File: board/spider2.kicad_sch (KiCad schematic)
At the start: 101 parts, among them J1 NRJ6HH, J10 PJ-320A, J11 PJ359, J12 PJ359, J13 PJ359, J14 PJ359, J15 PJ359, J16 PJ359, J19 PJ359, J2 NRJ6HH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

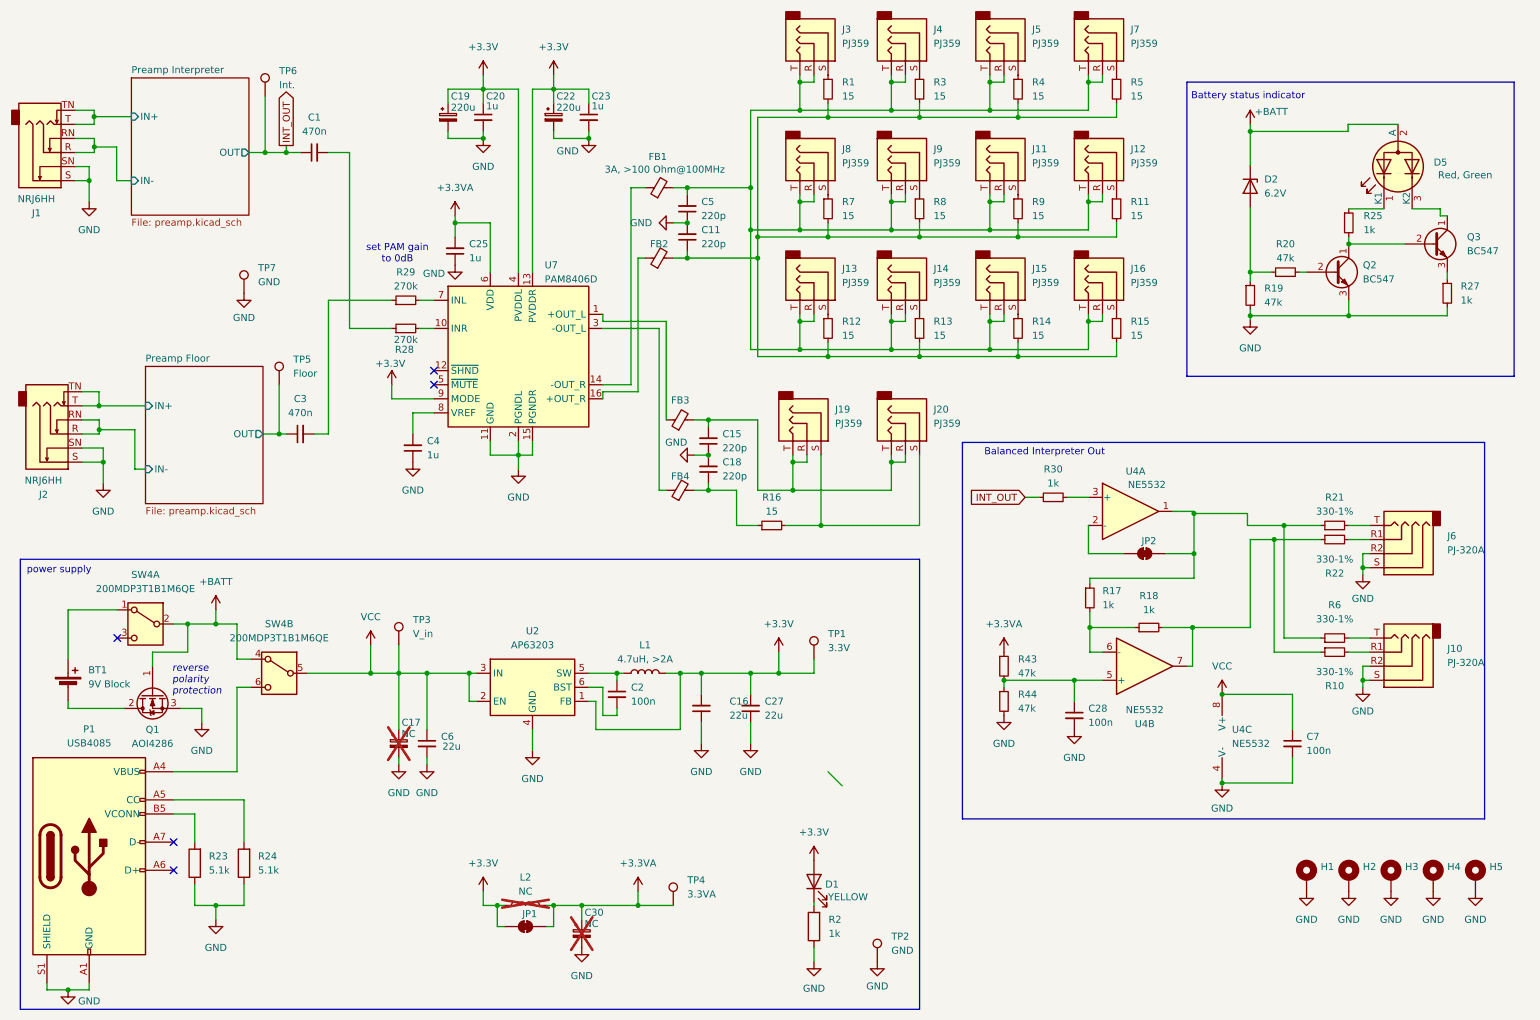
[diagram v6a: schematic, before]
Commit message: reduce balanced out volume, 3.3V supply on SMD for lower emissions
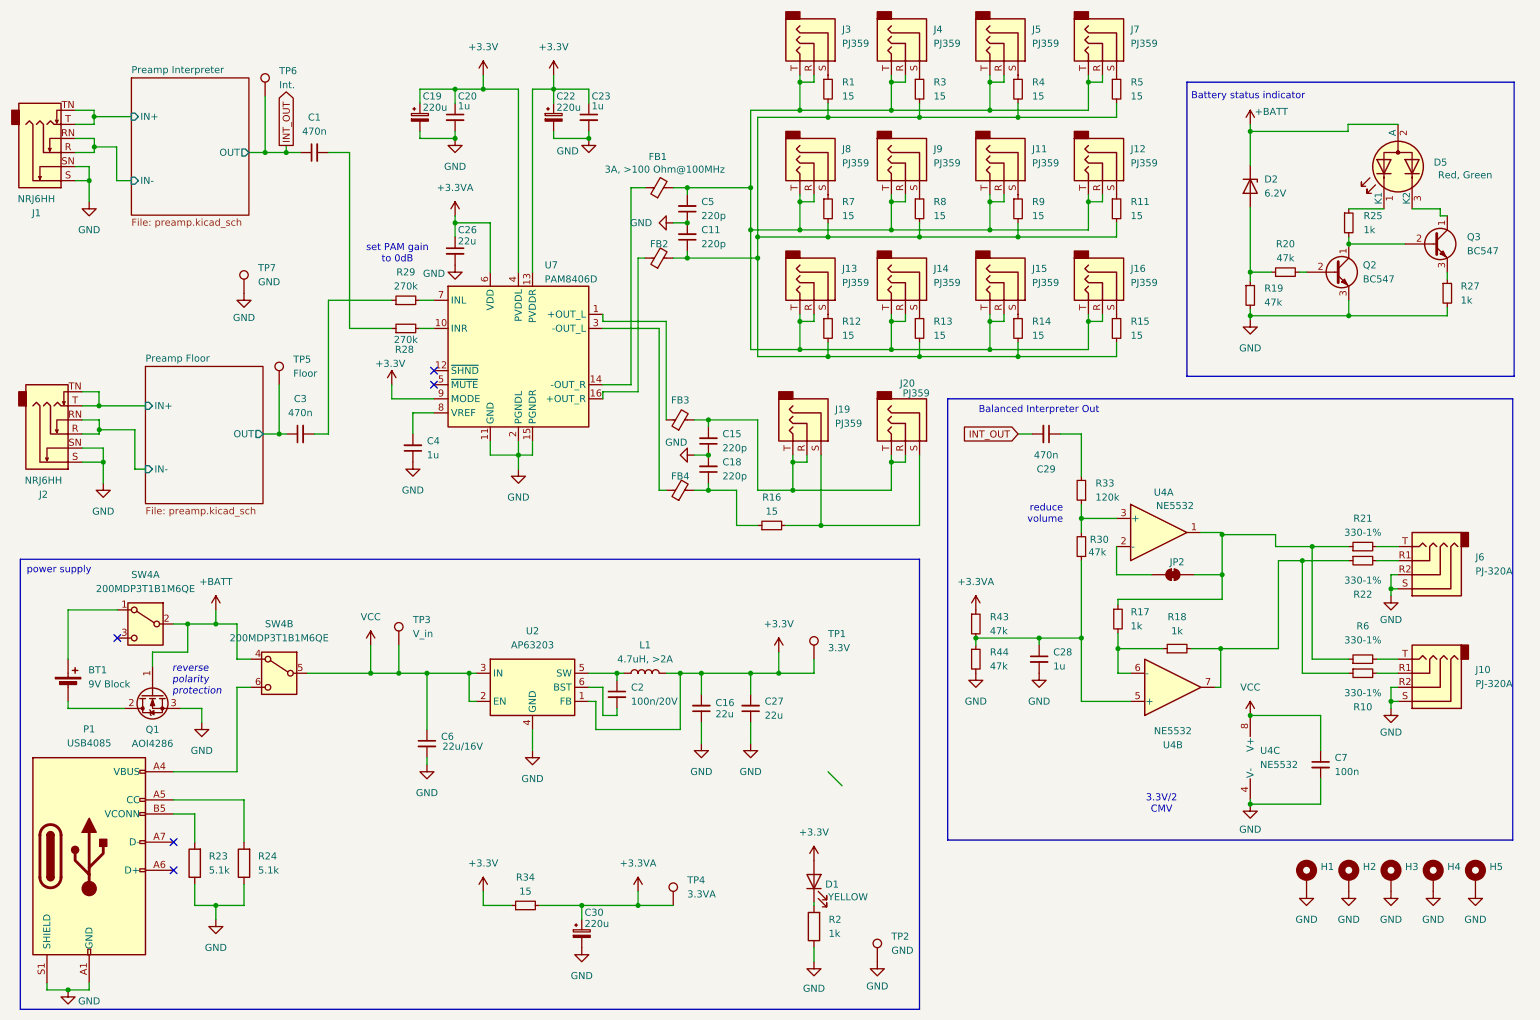
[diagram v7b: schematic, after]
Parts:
- removed C17: NC, Capacitor_THT:CP_Radial_D6.3mm_P2.50mm, symbol Device:C_Polarized_Small
- removed C25: 1u, Capacitor_THT:C_Disc_D4.3mm_W1.9mm_P5.00mm, symbol Device:C_Small
- removed JP1: SolderJumper_2_Bridged, Jumper:SolderJumper-2_P1.3mm_Bridged_RoundedPad1.0x1.5mm, symbol Jumper:SolderJumper_2_Bridged
- removed L2: NC, Inductor_THT:L_Axial_L5.3mm_D2.2mm_P10.16mm_Horizontal_Vishay_IM-1, symbol Device:L
- added C26: 22u, Capacitor_SMD:C_1206_3216Metric_Pad1.33x1.80mm_HandSolder, symbol Device:C_Small
- added C29: 470n, Capacitor_THT:C_Disc_D5.1mm_W3.2mm_P5.00mm, symbol Device:C_Small
- added R33: 120k, Resistor_THT:R_Axial_DIN0207_L6.3mm_D2.5mm_P10.16mm_Horizontal, symbol Device:R_Small
- added R34: 15, Resistor_THT:R_Axial_DIN0207_L6.3mm_D2.5mm_P10.16mm_Horizontal, symbol Device:R_Small
- C16, C27: footprint Capacitor_THT:C_Disc_D4.3mm_W1.9mm_P5.00mm -> Capacitor_SMD:C_1206_3216Metric_Pad1.33x1.80mm_HandSolder
- C2: value 100n -> 100n/20V; footprint Capacitor_THT:C_Disc_D5.1mm_W3.2mm_P5.00mm -> Capacitor_SMD:C_1206_3216Metric_Pad1.33x1.80mm_HandSolder
- C28: value 100n -> 1u
- C30: value NC -> 220u; now fitted
- C6: value 22u -> 22u/16V; footprint Capacitor_THT:C_Disc_D4.3mm_W1.9mm_P5.00mm -> Capacitor_SMD:C_1206_3216Metric_Pad1.33x1.80mm_HandSolder
- L1: footprint Inductor_THT:L_Radial_D8.7mm_P5.00mm_Fastron_07HCP -> Inductor_SMD:L_Bourns_SRN6045TA
- R30: value 1k -> 47k
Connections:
- net +3.3V: now also R34.1
- net +3.3VA: now also C26.1, R34.2
- net GND: now also C26.2
- net INT_OUT: now also C29.2; no longer R30.1
- net at C28.1, R43.2, R44.1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: now also R30.1
- net at R30.2, U4.3 (+): now also R33.1
- new net: C29.1, R33.2
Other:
- note added: "3.3V/2 CMV"
- note added: "reduce volume"
- moved on the sheet: C19, C20, C28, C7, J10, J6, JP2, R10, R17, R18, R21, R22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

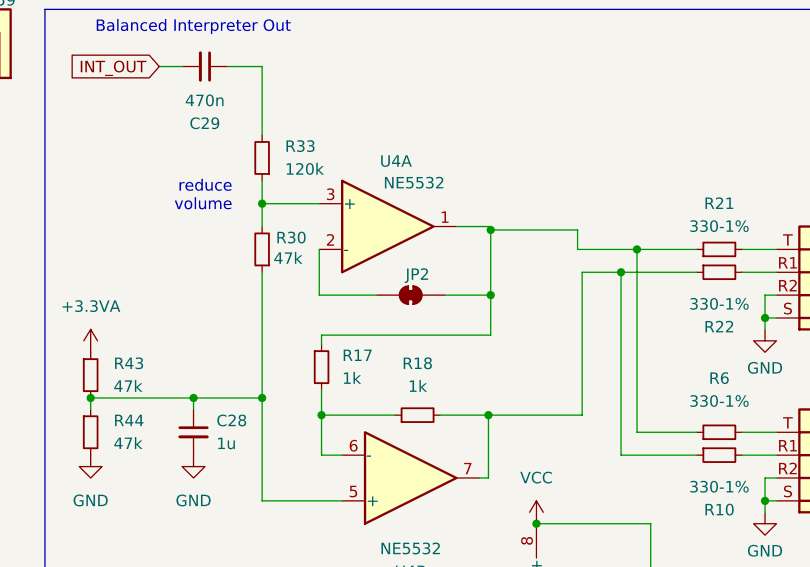
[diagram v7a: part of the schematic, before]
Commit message: rotate potentiometer by 180deg
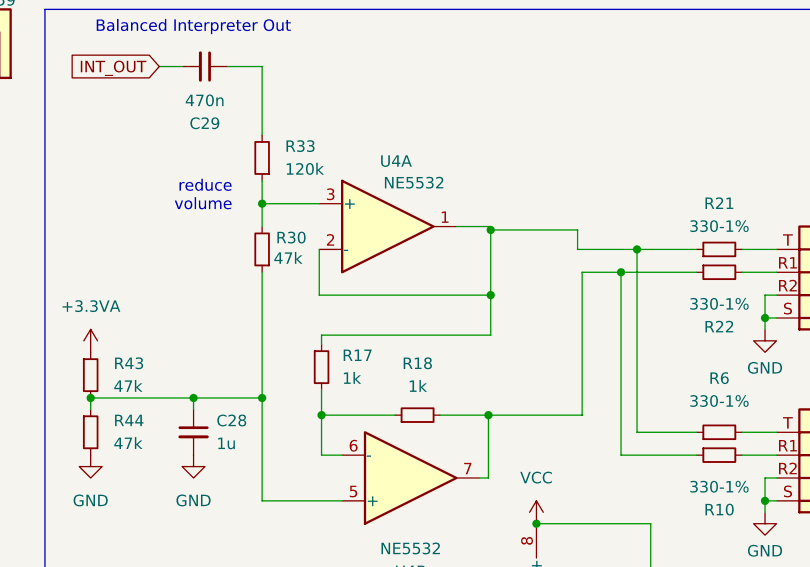
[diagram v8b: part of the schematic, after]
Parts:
- removed JP2: SolderJumper_2_Bridged, Jumper:SolderJumper-2_P1.3mm_Bridged_RoundedPad1.0x1.5mm, symbol Jumper:SolderJumper_2_Bridged
- C28, C7: footprint Capacitor_THT:C_Disc_D5.1mm_W3.2mm_P5.00mm -> Capacitor_THT:C_Disc_D4.3mm_W1.9mm_P5.00mm
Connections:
- net at R17.1, R21.1, R6.1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: now also U4.2 (-)
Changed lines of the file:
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@@
 	(wire
 		(pts
-			(xy 212.09 116.84) (xy 218.44 116.84)
+			(xy 212.09 116.84) (xy 231.14 116.84)
 		)
 		(stroke
@@
 	(wire
 		(pts
-			(xy 226.06 116.84) (xy 231.14 116.84)
-		)
-		(stroke
-			(width 0)
-			(type default)
-		)
-	)
-	(wire
-		(pts
 			(xy 205.74 109.22) (xy 205.74 106.68)
 		)
@@
 			)
 		)
-		(property "Footprint" "Capacitor_THT:C_Disc_D5.1mm_W3.2mm_P5.00mm"
+		(property "Footprint" "Capacitor_THT:C_Disc_D4.3mm_W1.9mm_P5.00mm"
 			(at 198.12 132.08 0)
 			(effects
@@
 			)
 		)
-		(property "Footprint" "Capacitor_THT:C_Disc_D5.1mm_W3.2mm_P5.00mm"
+		(property "Footprint" "Capacitor_THT:C_Disc_D4.3mm_W1.9mm_P5.00mm"
 			(at 248.92 151.13 0)
 			(effects
@@
 					(unit 1)
 				)
-			)
-		)
-	)
-	(symbol
-		(lib_id "Jumper:SolderJumper_2_Bridged")
-		(at 222.25 116.84 0)
-		(unit 1)
-		(exclude_from_sim yes)
-		(in_bom no)
-		(on_board yes)
-		(dnp no)
-		(property "Reference" "JP2"
-			(at 223.012 114.554 0)
-			(effects
-				(font
-					(size 1.27 1.27)
-				)
-			)
-		)
-		(property "Value" "SolderJumper_2_Bridged"
-			(at 222.25 113.03 0)
-			(effects
-				(font
-					(size 1.27 1.27)
-				)
-				(hide yes)
-			)
-		)
-		(property "Footprint" "Jumper:SolderJumper-2_P1.3mm_Bridged_RoundedPad1.0x1.5mm"
-			(at 222.25 116.84 0)
-			(effects
-				(font
-					(size 1.27 1.27)
-				)
-				(hide yes)
-			)
-		)
-		(property "Datasheet" "~"
-			(at 222.25 116.84 0)
-			(effects
-				(font
-					(size 1.27 1.27)
-				)
-				(hide yes)
-			)
-		)
-		(property "Description" "Solder Jumper, 2-pole, closed/bridged"
-			(at 222.25 116.84 0)
-			(effects
-				(font
-					(size 1.27 1.27)
-				)
-				(hide yes)
-			)
-		)
-		(property "Sim.Device" ""
-			(at 222.25 116.84 0)
-			(effects
-				(font
-					(size 1.27 1.27)
-				)
-				(hide yes)
-			)
-		)
-		(property "Sim.Pins" ""
-			(at 222.25 116.84 0)
-			(effects
-				(font
-					(size 1.27 1.27)
-				)
-				(hide yes)
-			)
-		)
-		(property "Sim.Type" ""
-			(at 222.25 116.84 0)
-			(effects
-				(font
-					(size 1.27 1.27)
-				)
-				(hide yes)
-			)
-		)
-		(pin "1"
-		)
-		(pin "2"
-		)
-		(instances
-			(project "spider2"
-				(path "/31073f88-a990-4ecc-8ab9-bb6b56c98e1e"
-					(reference "JP2")
-					(unit 1)
-				)
